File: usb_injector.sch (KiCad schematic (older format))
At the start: 10 parts, among them J1 USB_MALE, J2 USB_FEMALE, J3 USB_FEMALE_WITH_ID, J4 USB_FEMALE_WITH_ID, J5 USB_MALE, J6 USB_FEMALE, J7 USB_FEMALE_WITH_ID, J8 USB_FEMALE_WITH_ID, P1 CONN_6, P2 CONN_6

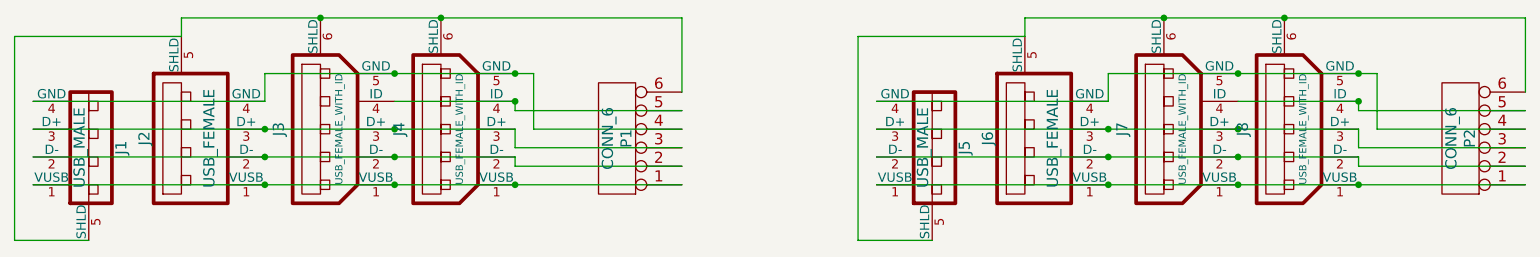
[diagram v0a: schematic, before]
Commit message: changed footprints to comply with KiCad Library Conventions and moved board/components so that the board aligns with a 5mm grid
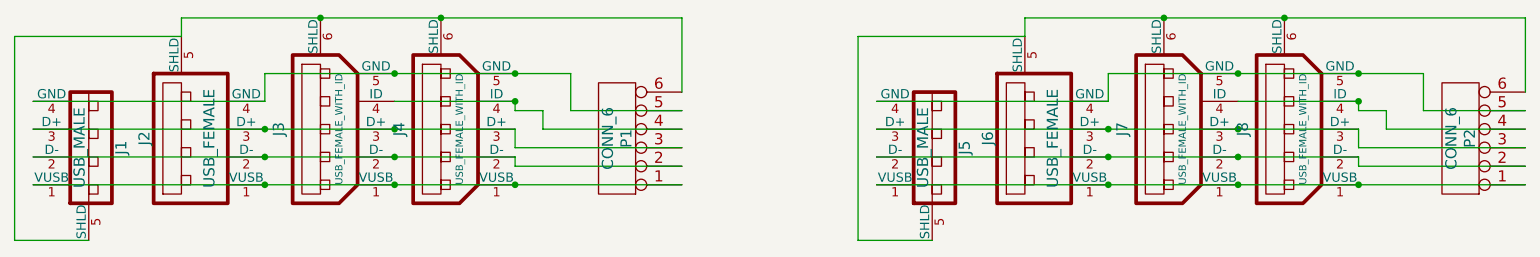
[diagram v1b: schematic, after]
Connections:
- net at J1.4 (GND), J2.4 (GND), J3.5 (GND)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: now also P1.5; no longer P1.4
- net at J3.4 (ID), J4.4 (ID): now also P1.4; no longer P1.5
- net at J5.4 (GND), J6.4 (GND), J7.5 (GND)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: now also P2.5; no longer P2.4
- net at J7.4 (ID), J8.4 (ID): now also P2.4; no longer P2.5
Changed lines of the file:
@@
 	3450 2150 3450 2000
 Wire Wire Line
-	3450 2000 4900 2000
+	3450 2000 5100 2000
 Connection ~ 4150 2000
 Wire Wire Line
@@
 Wire Wire Line
 	4800 2400 5700 2400
-Wire Wire Line
-	5700 2300 4900 2300
-Wire Wire Line
-	4900 2300 4900 2000
 Connection ~ 4800 2000
 Connection ~ 4800 2150
@@
 Wire Wire Line
 	4800 2150 4800 2200
-Wire Wire Line
-	4800 2200 5700 2200
 Wire Wire Line
 	4800 2150 4150 2150
@@
 	8000 2150 8000 2000
 Wire Wire Line
-	8000 2000 9450 2000
+	8000 2000 9700 2000
 Connection ~ 8700 2000
 Wire Wire Line
@@
 Wire Wire Line
 	9350 2400 10250 2400
-Wire Wire Line
-	10250 2300 9450 2300
-Wire Wire Line
-	9450 2300 9450 2000
 Connection ~ 9350 2000
 Connection ~ 9350 2150
@@
 	9350 2150 9350 2200
 Wire Wire Line
-	9350 2200 10250 2200
+	9350 2150 8700 2150
 Wire Wire Line
-	9350 2150 8700 2150
+	5700 2300 4950 2300
+Wire Wire Line
+	4950 2300 4950 2200
+Wire Wire Line
+	4950 2200 4800 2200
+Wire Wire Line
+	5100 2000 5100 2200
+Wire Wire Line
+	5100 2200 5700 2200
+Wire Wire Line
+	9350 2200 9500 2200
+Wire Wire Line
+	9500 2200 9500 2300
+Wire Wire Line
+	9500 2300 10250 2300
+Wire Wire Line
+	10250 2200 9700 2200
+Wire Wire Line
+	9700 2200 9700 2000
 $EndSCHEMATC

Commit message: updated components, fixed .1" headers spacing, rearranged header pinout such that full size USB-connectors have length-matched traces and moved USB-mini connector alongside USB-micro connector
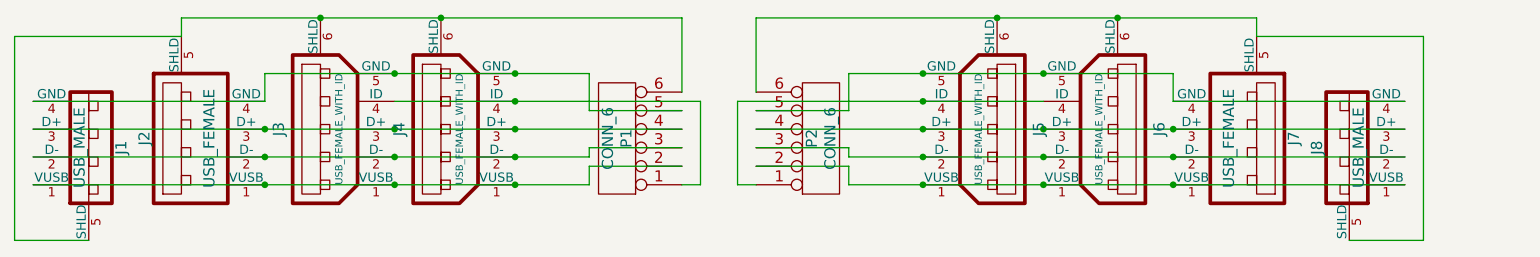
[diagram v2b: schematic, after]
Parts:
- removed J5: USB_MALE, symbol USB_MALE
- removed J6: USB_FEMALE, symbol USB_FEMALE
- removed J7, J8: USB_FEMALE_WITH_ID, symbol USB_FEMALE_WITH_ID
- added J5, J6: USB_FEMALE_WITH_ID, symbol USB_FEMALE_WITH_ID
- added J7: USB_FEMALE, symbol USB_FEMALE
- added J8: USB_MALE, symbol USB_MALE
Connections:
- net at J1.1 (VUSB), J2.1 (VUSB), J3.1 (VUSB)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: now also P1.2; no longer P1.1
- net at J1.2 (D-), J2.2 (D-), J3.2 (D-)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: now also P1.3; no longer P1.2
- net at J1.3 (D+), J2.3 (D+), J3.3 (D+)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: now also P1.4; no longer P1.3
- net at J3.4 (ID), J4.4 (ID): now also P1.1; no longer P1.4
- net at P2.1: now also J5.4 (ID), J6.4 (ID)
- net at P2.2: now also J5.1 (VUSB), J6.1 (VUSB), J7.1 (VUSB), J8.1 (VUSB)
- net at P2.3: now also J5.2 (D-), J6.2 (D-), J7.2 (D-), J8.2 (D-)
- net at P2.5: now also J5.5 (GND), J6.5 (GND), J7.4 (GND), J8.4 (GND)
- net at P2.6: now also J5.6 (SHLD), J6.6 (SHLD), J7.5 (SHLD), J8.5 (SHLD)
- net at P2.4: now also J5.3 (D+), J6.3 (D+), J7.3 (D+), J8.3 (D+)
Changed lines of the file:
@@
 LIBS:valves
 LIBS:connectors
-LIBS:rj45
 LIBS:usb_injector-cache
 EELAYER 25 0
@@
 	0    -1   -1   0
 $EndComp
-Wire Wire Line
-	2200 2600 5700 2600
 Connection ~ 3450 2600
 Connection ~ 4150 2600
 Wire Wire Line
-	2200 2450 4800 2450
+	2200 2450 5200 2450
 Connection ~ 4150 2450
 Connection ~ 3450 2450
 Wire Wire Line
-	2200 2300 4800 2300
+	2200 2300 5700 2300
 Connection ~ 4150 2300
 Connection ~ 3450 2300
@@
 	3450 2150 3450 2000
 Wire Wire Line
-	3450 2000 5100 2000
+	3450 2000 5200 2000
 Connection ~ 4150 2000
 Wire Wire Line
@@
 $EndComp
 Connection ~ 4800 2600
-Wire Wire Line
-	5700 2500 4800 2500
-Wire Wire Line
-	4800 2500 4800 2450
-Wire Wire Line
-	4800 2300 4800 2400
-Wire Wire Line
-	4800 2400 5700 2400
 Connection ~ 4800 2000
 Connection ~ 4800 2150
+Connection ~ 4400 1700
+Wire Wire Line
+	4150 2150 5800 2150
+Wire Wire Line
+	2200 2600 5200 2600
+Wire Wire Line
+	5200 2600 5200 2500
+Wire Wire Line
+	5200 2500 5700 2500
+Wire Wire Line
+	5200 2450 5200 2400
+Wire Wire Line
+	5200 2400 5700 2400
+Connection ~ 4800 2450
+Connection ~ 4800 2300
+Wire Wire Line
+	5800 2150 5800 2600
+Wire Wire Line
+	5800 2600 5700 2600
+Wire Wire Line
+	5200 2000 5200 2200
+Wire Wire Line
+	5200 2200 5700 2200
 Wire Wire Line
 	5700 1700 5700 2100
-Connection ~ 4400 1700
-Wire Wire Line
-	4800 2150 4800 2200
-Wire Wire Line
-	4800 2150 4150 2150
-$Comp
-L USB_FEMALE J6
-U 1 1 54AF3FDA
-P 7550 2350
-F 0 "J6" H 7550 2550 60  0000 C CNN
-F 1 "USB_FEMALE" H 7550 2200 60  0000 C CNN
-F 2 "" H 6750 2300 60  0000 C CNN
-F 3 "" H 6750 2300 60  0000 C CNN
-	1    7550 2350
-	0    -1   -1   0
-$EndComp
-$Comp
-L USB_MALE J5
-U 1 1 54AF3FE0
-P 7050 2400
-F 0 "J5" H 7050 2575 60  0000 C CNN
-F 1 "USB_MALE" H 7050 2350 60  0000 C CNN
-F 2 "" H 6250 2350 60  0000 C CNN
-F 3 "" H 6250 2350 60  0000 C CNN
-	1    7050 2400
-	0    1    1    0
-$EndComp
-$Comp
-L USB_FEMALE_WITH_ID J7
-U 1 1 54AF3FE6
-P 8300 2300
-F 0 "J7" H 8300 2525 60  0000 C CNN
-F 1 "USB_FEMALE_WITH_ID" H 8300 2200 39  0000 C CNN
-F 2 "" H 7500 2250 60  0000 C CNN
-F 3 "" H 7500 2250 60  0000 C CNN
-	1    8300 2300
-	0    -1   -1   0
-$EndComp
-$Comp
-L USB_FEMALE_WITH_ID J8
-U 1 1 54AF3FEC
-P 8950 2300
-F 0 "J8" H 8950 2525 60  0000 C CNN
-F 1 "USB_FEMALE_WITH_ID" H 8950 2200 39  0000 C CNN
-F 2 "" H 8150 2250 60  0000 C CNN
-F 3 "" H 8150 2250 60  0000 C CNN
-	1    8950 2300
-	0    -1   -1   0
-$EndComp
-Wire Wire Line
-	6750 2600 10250 2600
-Connection ~ 8000 2600
-Connection ~ 8700 2600
-Wire Wire Line
-	6750 2450 9350 2450
-Connection ~ 8700 2450
-Connection ~ 8000 2450
-Wire Wire Line
-	6750 2300 9350 2300
-Connection ~ 8700 2300
-Connection ~ 8000 2300
-Wire Wire Line
-	6750 2150 8000 2150
-Wire Wire Line
-	8000 2150 8000 2000
-Wire Wire Line
-	8000 2000 9700 2000
-Connection ~ 8700 2000
-Wire Wire Line
-	7050 2900 6650 2900
-Wire Wire Line
-	6650 2900 6650 1800
-Wire Wire Line
-	6650 1800 7550 1800
-Wire Wire Line
-	7550 1800 7550 1700
-Wire Wire Line
-	7550 1700 10250 1700
-Connection ~ 8300 1700
+$Comp
+L USB_FEMALE J7
+U 1 1 54D6C05A
+P 8800 2350
+F 0 "J7" H 8800 2550 60  0000 C CNN
+F 1 "USB_FEMALE" H 8800 2200 60  0000 C CNN
+F 2 "" H 8000 2300 60  0000 C CNN
+F 3 "" H 8000 2300 60  0000 C CNN
+	1    8800 2350
+	0    1    -1   0
+$EndComp
+$Comp
+L USB_MALE J8
+U 1 1 54D6C060
+P 9300 2400
+F 0 "J8" H 9300 2575 60  0000 C CNN
+F 1 "USB_MALE" H 9300 2350 60  0000 C CNN
+F 2 "" H 8500 2350 60  0000 C CNN
+F 3 "" H 8500 2350 60  0000 C CNN
+	1    9300 2400
+	0    -1   1    0
+$EndComp
+$Comp
+L USB_FEMALE_WITH_ID J6
+U 1 1 54D6C066
+P 8050 2300
+F 0 "J6" H 8050 2525 60  0000 C CNN
+F 1 "USB_FEMALE_WITH_ID" H 8050 2200 39  0000 C CNN
+F 2 "" H 7250 2250 60  0000 C CNN
+F 3 "" H 7250 2250 60  0000 C CNN
+	1    8050 2300
+	0    1    -1   0
+$EndComp
+$Comp
+L USB_FEMALE_WITH_ID J5
+U 1 1 54D6C06C
+P 7400 2300
+F 0 "J5" H 7400 2525 60  0000 C CNN
+F 1 "USB_FEMALE_WITH_ID" H 7400 2200 39  0000 C CNN
+F 2 "" H 6600 2250 60  0000 C CNN
+F 3 "" H 6600 2250 60  0000 C CNN
+	1    7400 2300
+	0    1    -1   0
+$EndComp
+Connection ~ 8350 2600
+Connection ~ 7650 2600
+Wire Wire Line
+	9600 2450 6600 2450
+Connection ~ 7650 2450
+Connection ~ 8350 2450
+Wire Wire Line
+	9600 2300 6100 2300
+Connection ~ 7650 2300
+Connection ~ 8350 2300
+Wire Wire Line
+	9600 2150 8350 2150
+Wire Wire Line
+	8350 2150 8350 2000
+Wire Wire Line
+	8350 2000 6600 2000
+Connection ~ 7650 2000
+Wire Wire Line
+	9300 2900 9700 2900
+Wire Wire Line
+	9700 2900 9700 1800
+Wire Wire Line
+	9700 1800 8800 1800
+Wire Wire Line
+	8800 1800 8800 1700
+Wire Wire Line
+	8800 1700 6100 1700
+Connection ~ 8050 1700
 $Comp
 L CONN_6 P2
-U 1 1 54AF4005
-P 9900 2350
-F 0 "P2" V 9850 2350 60  0000 C CNN
-F 1 "CONN_6" V 9950 2350 60  0000 C CNN
-F 2 "" H 9900 2350 60  0000 C CNN
-F 3 "" H 9900 2350 60  0000 C CNN
-	1    9900 2350
-	-1   0    0    1
-$EndComp
-Connection ~ 9350 2600
-Wire Wire Line
-	10250 2500 9350 2500
-Wire Wire Line
-	9350 2500 9350 2450
-Wire Wire Line
-	9350 2300 9350 2400
-Wire Wire Line
-	9350 2400 10250 2400
-Connection ~ 9350 2000
-Connection ~ 9350 2150
-Wire Wire Line
-	10250 1700 10250 2100
-Connection ~ 8950 1700
-Wire Wire Line
-	9350 2150 9350 2200
-Wire Wire Line
-	9350 2150 8700 2150
-Wire Wire Line
-	5700 2300 4950 2300
-Wire Wire Line
-	4950 2300 4950 2200
-Wire Wire Line
-	4950 2200 4800 2200
-Wire Wire Line
-	5100 2000 5100 2200
-Wire Wire Line
-	5100 2200 5700 2200
-Wire Wire Line
-	9350 2200 9500 2200
-Wire Wire Line
-	9500 2200 9500 2300
-Wire Wire Line
-	9500 2300 10250 2300
-Wire Wire Line
-	10250 2200 9700 2200
-Wire Wire Line
-	9700 2200 9700 2000
+U 1 1 54D6C084
+P 6450 2350
+F 0 "P2" V 6400 2350 60  0000 C CNN
+F 1 "CONN_6" V 6500 2350 60  0000 C CNN
+F 2 "" H 6450 2350 60  0000 C CNN
+F 3 "" H 6450 2350 60  0000 C CNN
+	1    6450 2350
+	1    0    0    1
+$EndComp
+Connection ~ 7000 2600
+Connection ~ 7000 2000
+Connection ~ 7000 2150
+Connection ~ 7400 1700
+Wire Wire Line
+	7650 2150 6000 2150
+Wire Wire Line
+	6600 2600 9600 2600
+Wire Wire Line
+	6600 2600 6600 2500
+Wire Wire Line
+	6600 2500 6100 2500
+Wire Wire Line
+	6600 2450 6600 2400
+Wire Wire Line
+	6600 2400 6100 2400
+Connection ~ 7000 2450
+Connection ~ 7000 2300
+Wire Wire Line
+	6000 2150 6000 2600
+Wire Wire Line
+	6000 2600 6100 2600
+Wire Wire Line
+	6600 2000 6600 2200
+Wire Wire Line
+	6600 2200 6100 2200
+Wire Wire Line
+	6100 1700 6100 2100
 $EndSCHEMATC
